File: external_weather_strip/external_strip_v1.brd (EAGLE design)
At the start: 100 x 80 mm, 10 parts, among them U1 ML8511-UV-SENSOR, U2 SHT21, U9 BMP180

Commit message: layouting 0.4
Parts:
- added U$5: MCP3425, phMeter:SOT-23-6
- moved C3 76.4 mm to (50.8, 7.62)
- moved U2 62.0 mm to (43.2, 6.35)
- moved C11 50.3 mm to (11.4, 3.81), turned to 90 degrees
- moved C12 47.7 mm to (14.0, 5.08), turned to 270 degrees
- moved U1 45.7 mm to (30.5, 7.62), turned to 90 degrees
- moved R1 44.7 mm to (25.4, 7.62)
- moved C1 44.6 mm to (25.4, 5.08)
- moved C2 41.9 mm to (26.7, 11.4)
- moved U9 37.9 mm to (7.62, 5.08), turned to 180 degrees
- moved JP2 25.4 mm to (2.54, 2.54), turned to 90 degrees
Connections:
- net ENABLE: no longer JP2.4
- net OUT: no longer JP2.3
- net SCL: now also JP2.4
- net SDA: now also JP2.3
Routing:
- net 3.3V: track 0.00 -> 31.0 mm
- net SCL: track 0.00 -> 20.7 mm, vias 0 -> 2
- net SDA: track 0.00 -> 20.4 mm
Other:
- board size 100 x 80 mm -> 100 x 12.7 mm

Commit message: finished weather strip
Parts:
- removed JP2: (no value), SparkFun-Connectors:1X04
- added C4: 100n, rcl:C0603
- added JP1: (no value), Headerlibrary:1X05
- R1: value 10K -> 10k; device SparkFun-Resistors:0603-RES -> resistor:R0603
- moved C3 30.6 mm to (20.3, 4.45), turned to 180 degrees
- moved U2 24.2 mm to (19.1, 7.62)
- moved U$5 16.7 mm to (29.2, 7.62), turned to 90 degrees
- moved R1 8.98 mm to (31.8, 14.0), turned to 90 degrees
- moved C1 7.75 mm to (31.8, 9.53), turned to 90 degrees
- moved C2 7.65 mm to (26.0, 3.81), turned to 270 degrees
- moved U1 3.24 mm to (29.8, 4.45)
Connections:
- removed net 3.3V: C2.1, JP2.1, R1.2, U1.7
- removed net ENABLE: R1.1, U1.4
- removed net OUT: U1.8
- new net N$1: U$5.VIN+, U1.8
- new net UV_EN: JP1.5, R1.1, U1.4
- net +3V3: now also C2.1, C4.1, JP1.1, U$5.VDD, U1.7
- net GND: now also C4.2, JP1.2, R1.2, U$5.VIN-, U$5.VSS; no longer JP2.2
- net SCL: now also JP1.4, U$5.SCL; no longer JP2.4
- net SDA: now also JP1.3, U$5.SDA; no longer JP2.3
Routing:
- net +3V3: track 0.00 -> 48.9 mm
- net UV_EN: track 0.00 -> 47.8 mm
- net 3.3V: track 31.0 -> 0.00 mm
- net SCL: track 20.7 -> 37.7 mm, vias 2 -> 4
- net SDA: track 20.4 -> 30.9 mm
- net N$3: track 0.00 -> 3.14 mm
- net N$1: track 0.00 -> 2.59 mm
- added copper zone on layer 1, net GND
- added copper zone on layer 16, net GND
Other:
- board size 100 x 12.7 mm -> 35.2 x 15.2 mm
- board text added: "3V3 GND SDA SCL UVEN"
- board text added: "MCP3425"
- board text added: "ML8511"
- board text added: "Octanis 1 weather monitor v1"
- board text added: "www.octanis.org"

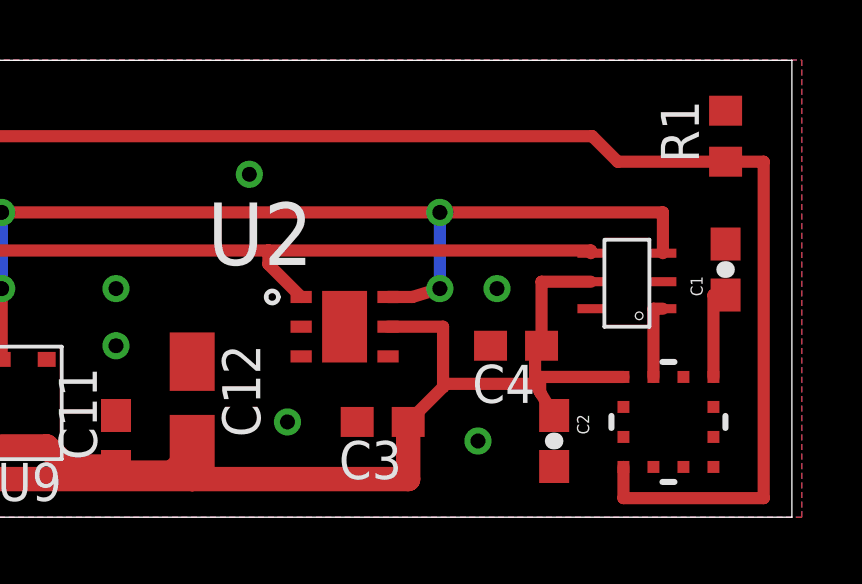
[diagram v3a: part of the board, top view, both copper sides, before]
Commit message: corrected UV sensor footprint
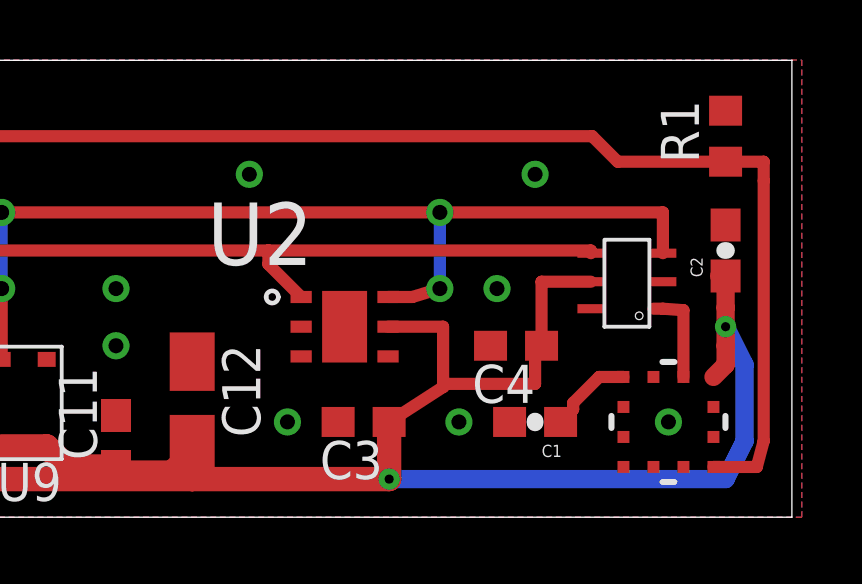
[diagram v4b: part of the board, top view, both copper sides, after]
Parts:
- removed U1: ML8511-UV-SENSOR, ML8511:ML8511
- added U3: ML8511-UV-SENSORSMD, SparkFun-Sensors:ML8511
- moved C2 8.54 mm to (31.8, 10.2), turned to 90 degrees
- moved C1 8.13 mm to (25.4, 4.45), turned to 180 degrees
- moved C3 0.64 mm to (19.7, 4.45)
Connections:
- net +3V3: now also U3.7; no longer U1.7
- net GND: now also U3.5; no longer U1.5
- net N$1: now also U3.8; no longer U1.8
- net N$3: now also U3.10; no longer U1.10
- net UV_EN: now also U3.4; no longer U1.4
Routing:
- net +3V3: track 48.9 -> 64.6 mm, vias 0 -> 2
- net UV_EN: track 47.8 -> 42.5 mm
- net N$1: track 2.59 -> 3.23 mm

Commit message: finished weather strip
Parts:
- added BLP, RST: PTR1B1,27, testpad:B1,27
- added C10: 12p, rcl:C0603
- added C13: 10u, rcl:C0603
- added C14: 670p, rcl:C0603
- added C15: 270p, rcl:C0603
- added C16: 10uF, SparkFun-Retired:EIA3216
- added C5: 1n, SparkFun-Capacitors:0603-CAP
- added C6, C7, C8: 100n, rcl:C0603
- added C9: 120n, rcl:C0603
- added IC1: AS3935, AS3935:16LDMLPQ
- added IC2: BNO055A, BNO055:BNO055
- added L1: 100uH, AS3935:COILCRAFT
- added Q1: 32.768kHz, crystal:FC-12M
- added R2, R3: 10k, rcl:R0603
- added R4: 10k, resistor:R0603
- C1: value 1nF -> 100n; device SparkFun-Capacitors:0603-CAP -> rcl:C0603
- C11: value 100n -> 12p
- C12: value 10u -> 1u; device resistor:A/3216-18R -> rcl:C0603
- C2: value 0.1uF -> 100n; device SparkFun-Capacitors:0603-CAP -> rcl:C0603
- C4: device rcl:C0603 -> SparkFun-Capacitors:0603-CAP
- JP1: device Headerlibrary:1X05 -> pinhead:1X07
- moved C12 34.7 mm to (46.6, 16.8)
- moved C1 20.4 mm to (5.08, 3.17), turned to 90 degrees
- moved C2 19.7 mm to (12.7, 5.08)
- moved C11 18.1 mm to (28.7, 9.45), turned to 180 degrees
- moved R1 13.6 mm to (22.9, 3.66), turned to 180 degrees
- moved U2 10.8 mm to (9.53, 12.7)
- moved U3 9.44 mm to (21.0, 7.62)
- moved U$5 8.84 mm to (21.0, 10.8)
- moved C3 8.28 mm to (12.7, 8.89), turned to 270 degrees
- moved C4 3.11 mm to (24.3, 10.1), turned to 90 degrees
- moved U9 1.42 mm to (8.89, 5.71)
- moved JP1 1.23 mm to (2.00, 10.0)
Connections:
- new net ACCEL_IRQ: IC2.14, JP1.7
- new net ACCEL_N_BOOTLD: BLP.TP, IC2.4, R3.1
- new net ACCEL_N_RST: IC2.11, R2.2, RST.TP
- new net LIGHTNING_IRQ: IC1.10, JP1.6
- new net N$18: C7.2, IC2.9
- new net N$19: C10.1, IC2.27, Q1.2
- new net N$2: C13.2, IC1.1
- new net N$5: C14.1, C15.1, IC1.3, L1.1, R4.2
- new net N$73: C11.1, IC2.26, Q1.1
- net +3V3: now also C1.1, C12.2, C16.A, C6.1, C8.1, C9.1, IC1.15, IC1.16, IC1.5, IC1.6, IC1.9, IC2.17, IC2.28, IC2.3, R2.1, R3.2; no longer C11.1, C12.+
- net GND: now also C10.2, C12.1, C13.1, C14.2, C15.2, C16.C, C5.2, C6.2, C7.1, C8.2, C9.2, IC1.2, IC1.4, IC1.7, IC1.EXP, IC2.10, IC2.15, IC2.16, IC2.18, IC2.2, IC2.25, IC2.5, IC2.6, L1.2, R4.1; no longer C12.-
- net N$3: now also C5.1; no longer C1.1
- net SCL: now also IC1.11, IC2.19
- net SDA: now also IC1.13, IC2.20
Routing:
- net +3V3: track 64.6 -> 173.3 mm
- net LIGHTNING_IRQ: track 0.00 -> 54.0 mm, vias 0 -> 3
- net ACCEL_IRQ: track 0.00 -> 41.2 mm
- net SDA: track 30.9 -> 63.1 mm, vias 0 -> 4
- net GND: track 0.00 -> 26.5 mm, vias 9 -> 21
- net SCL: track 37.7 -> 63.4 mm
- net N$5: track 0.00 -> 15.8 mm
- net ACCEL_N_RST: track 0.00 -> 5.45 mm
- net N$2: track 0.00 -> 5.28 mm
- net ACCEL_N_BOOTLD: track 0.00 -> 5.04 mm
- net N$73: track 0.00 -> 4.92 mm
- net N$19: track 0.00 -> 4.67 mm
- net N$3: track 2.84 -> 6.62 mm
- net N$18: track 0.00 -> 2.98 mm
- net UV_EN: track 42.5 -> 40.2 mm, vias 0 -> 2
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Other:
- board size 35.2 x 15.2 mm -> 60 x 18 mm

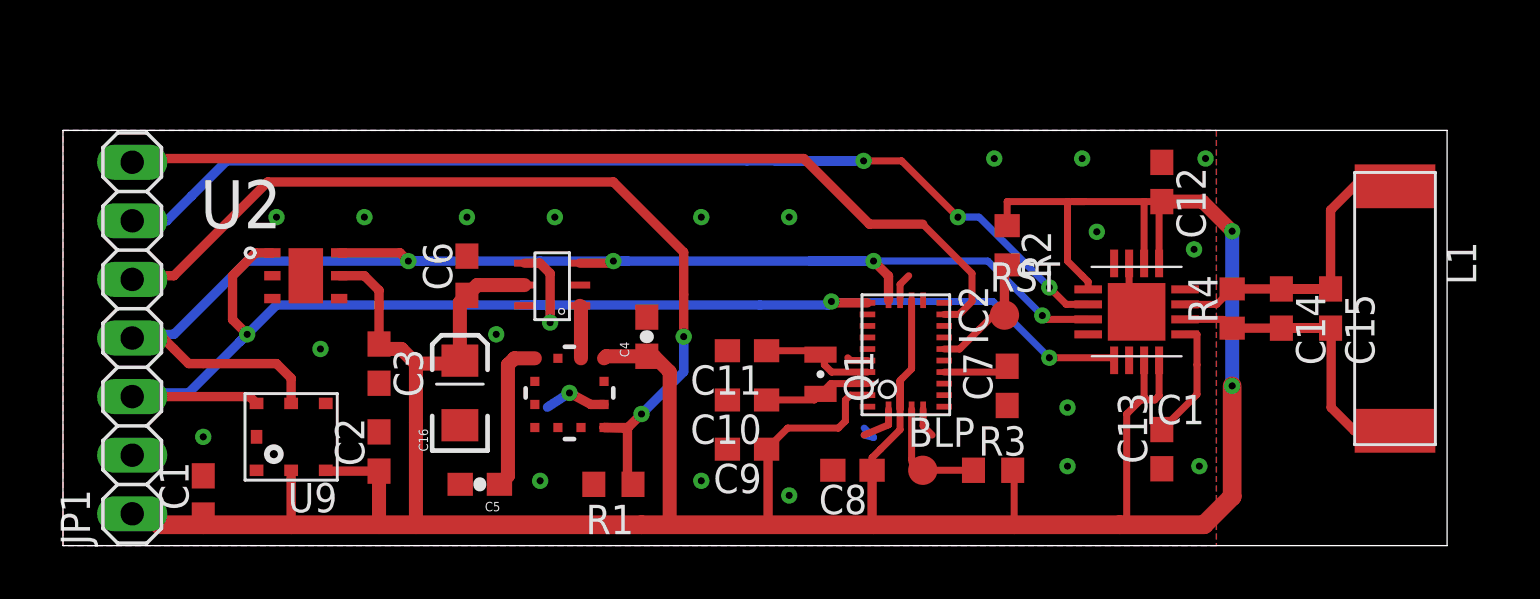
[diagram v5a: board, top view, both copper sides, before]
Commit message: finished revised weather strip
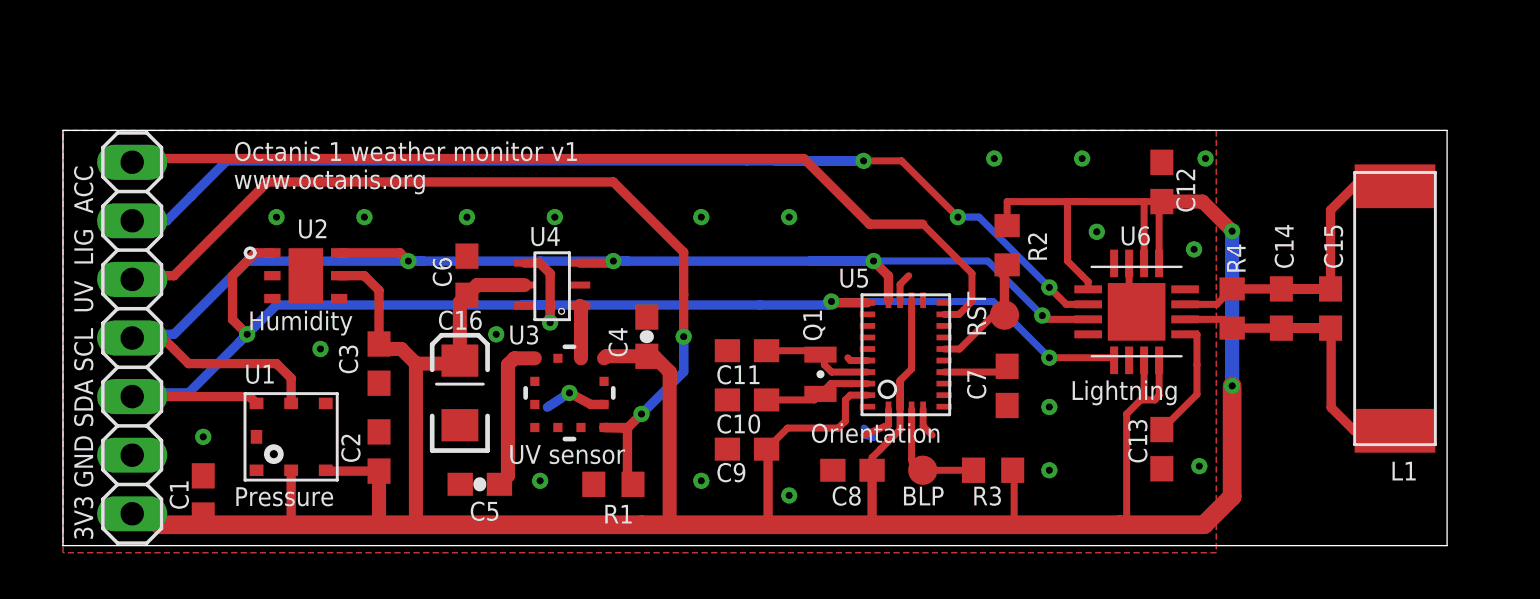
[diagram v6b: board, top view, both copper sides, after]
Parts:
- renumbered IC1 to U6, IC2 to U5, U$5 to U4, U9 to U1
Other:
- board text added: "3V3 GND SDA SCL UV LIG ACC"
- board text added: "Humidity"
- board text added: "Lightning"
- board text added: "Orientation"
- board text added: "Pressure"
- board text added: "U3"
- board text added: "U4"
- board text added: "UV sensor"
- board text removed: "3V3 GND SDA SCL UVEN"
